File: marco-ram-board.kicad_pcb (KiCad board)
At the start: 4 copper layers, 160 x 100 mm, 185 parts, among them J201 PRG_USB, J202 MCU_RST, J203 MCU_BOOT0, J204 FT_TXD, J205 FT_RXD, J206 CONN_JTAG, J301 CONN_MCU_SERIAL, J302 CONN_EXT, J501 MCU_USB, J502 SD_Card, J503 CONN_DISP, J504 RJ45_Amphenol_RJMG1BD3B8K1ANR, J601 CONN_JACK_12V, J602 CONN_SCREW_12V, Q201 MMBT3906, Q601 DMP3037LSS, SW301 SW_RST, SW302 SW_BOOT0, SW501 BTN0, SW502 BTN1, SW503 BTN2, SW504 BTN3, SW601 PWR_SW, U201 FT2232HL, U301 STM32F765IITx, U401 IS42S86400D, U402 IS42S86400D, U403 IS42S86400D, U404 IS42S86400D, U405 IS42S86400D, U406 IS42S86400D, U407 IS42S86400D, U408 IS42S86400D, U501 KSZ8081RNA, U601 LM2576S-3.3, Y201 12MHz, Y301 25MHz

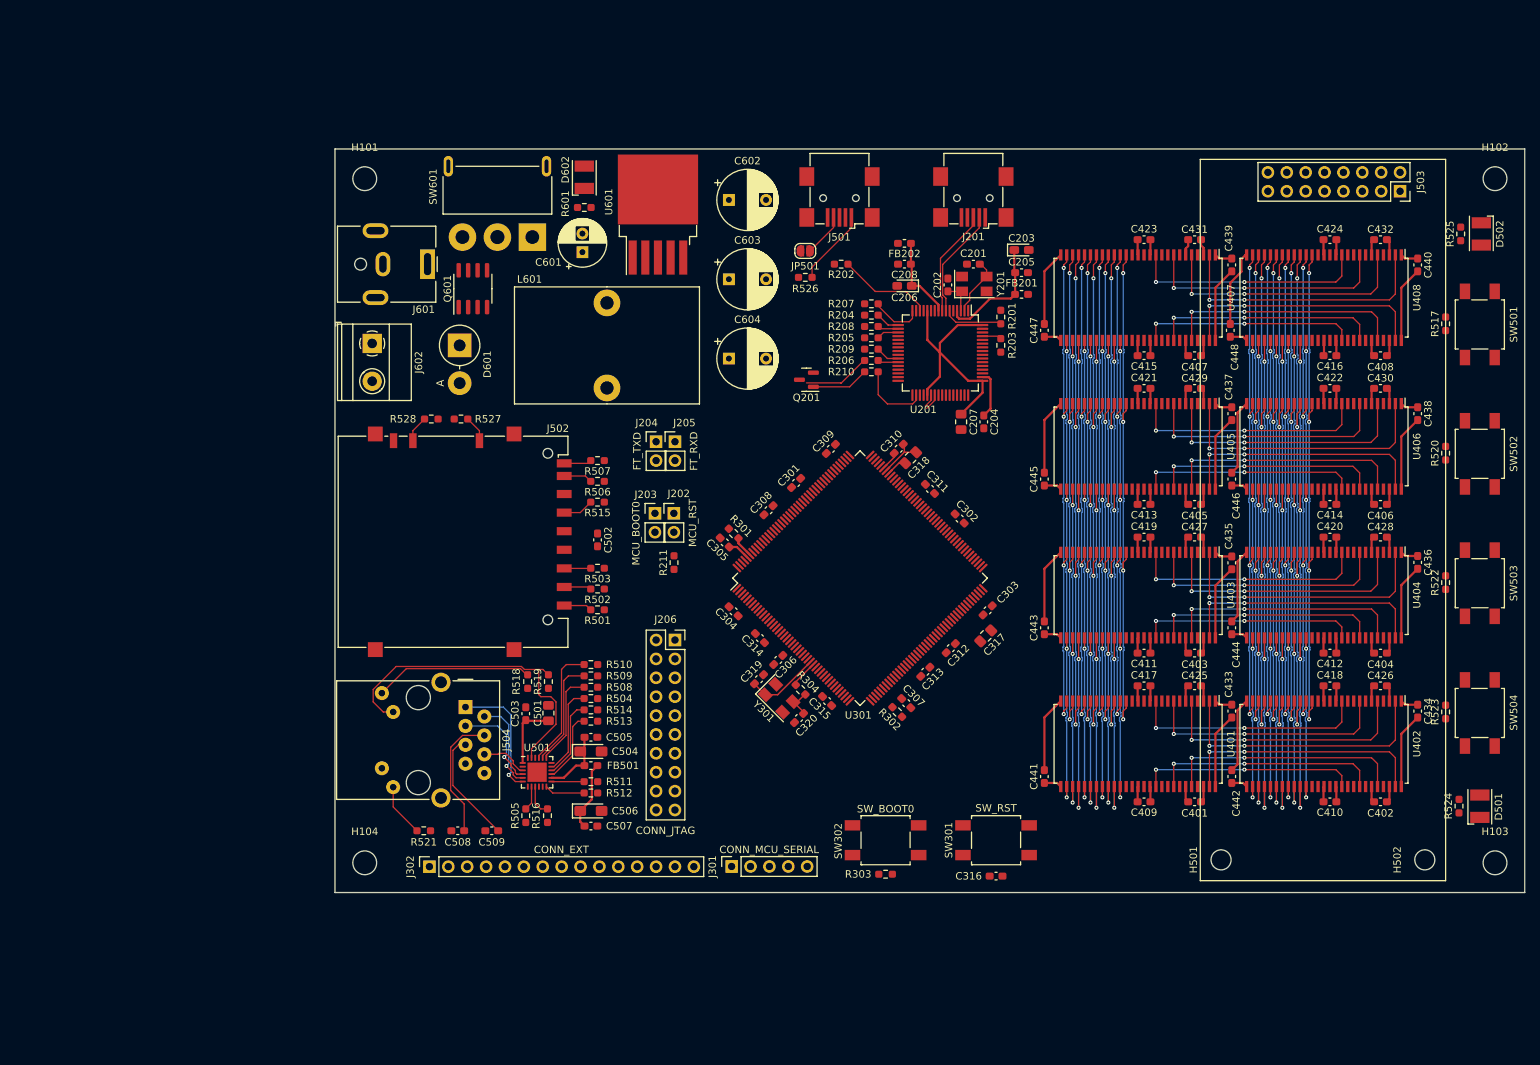
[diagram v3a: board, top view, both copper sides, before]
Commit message: Small placement modifications, change most routing to .2mm, more RAM routing
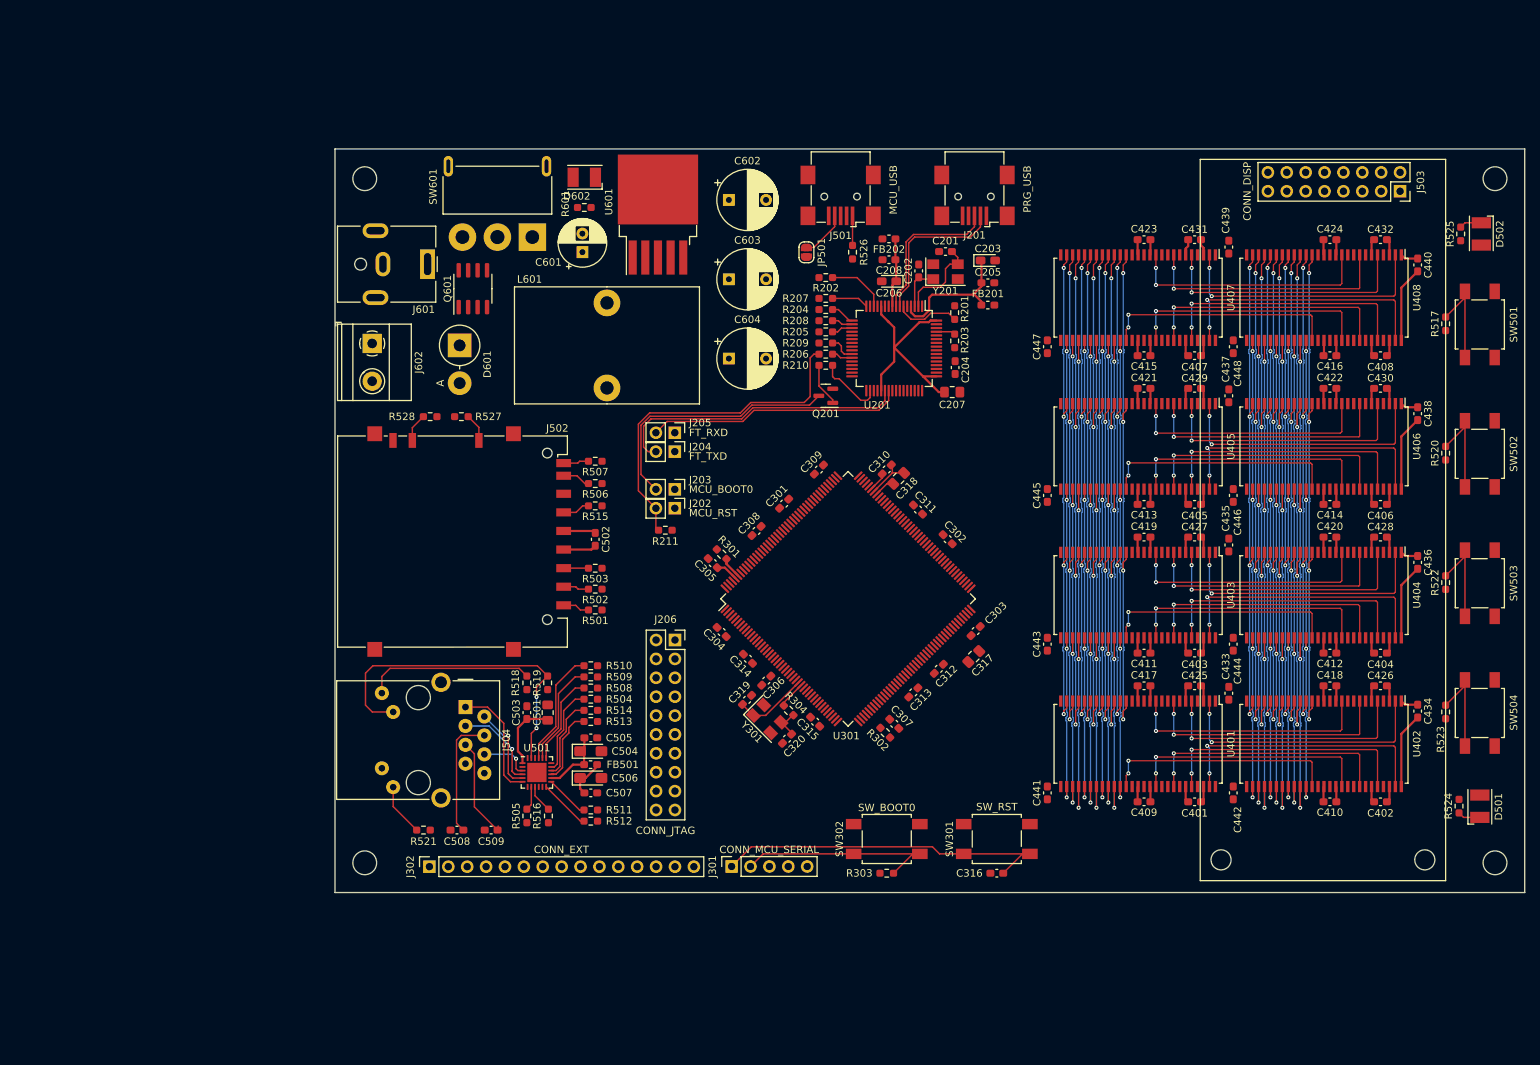
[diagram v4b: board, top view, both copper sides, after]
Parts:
- moved C204 8.26 mm to (153.4, 69.4)
- moved R526 7.20 mm to (139.6, 53.9), turned to 90 degrees
- moved U201 6.23 mm to (145.2, 66.8)
- moved R201 6.23 mm to (153.3, 62.0)
- moved R203 6.23 mm to (153.3, 65.8)
- moved R210 6.20 mm to (136.0, 69.1)
- moved R206 6.19 mm to (136.0, 67.6)
- moved R209 6.19 mm to (136.0, 66.1)
- moved R205 6.19 mm to (136.0, 64.6)
- moved R208 6.18 mm to (136.0, 63.1)
- moved R204 6.18 mm to (136.0, 61.6)
- moved R207 6.18 mm to (136.0, 60.1)
- moved FB201 4.75 mm to (157.8, 61.0)
- moved C203 4.74 mm to (157.8, 55.0)
- moved C205 4.73 mm to (157.8, 58.0)
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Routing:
- net VDD: track 189.9 -> 95.6 mm
- net GND: track 174.2 -> 117.9 mm
- net /mcu/~{RESET}: track 0.00 -> 46.3 mm
- net Net-(J204-Pad2): track 1.11 -> 39.9 mm
- net Net-(J202-Pad2): track 8.99 -> 46.6 mm
- net Net-(J203-Pad2): track 0.00 -> 35.0 mm
- net Net-(J205-Pad2): track 1.53 -> 34.4 mm
- net /mcu/SDRAM.~{BL1}: track 0.00 -> 31.6 mm, vias 0 -> 2
- net /mcu/SDRAM.~{BL0}: track 0.00 -> 31.6 mm, vias 0 -> 2
- net /mcu/SDRAM.~{BL3}: track 0.00 -> 31.6 mm, vias 0 -> 2
- net /mcu/SDRAM.~{BL2}: track 0.00 -> 31.6 mm, vias 0 -> 2
- net /mcu/BOOT0: track 0.00 -> 28.1 mm
- net /mcu-if/BTN2: track 0.00 -> 13.4 mm
- net /mcu-if/BTN0: track 0.00 -> 13.4 mm
- net /mcu-if/BTN1: track 0.00 -> 13.4 mm
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
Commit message: Finish RAM routing (except connections to MCU).
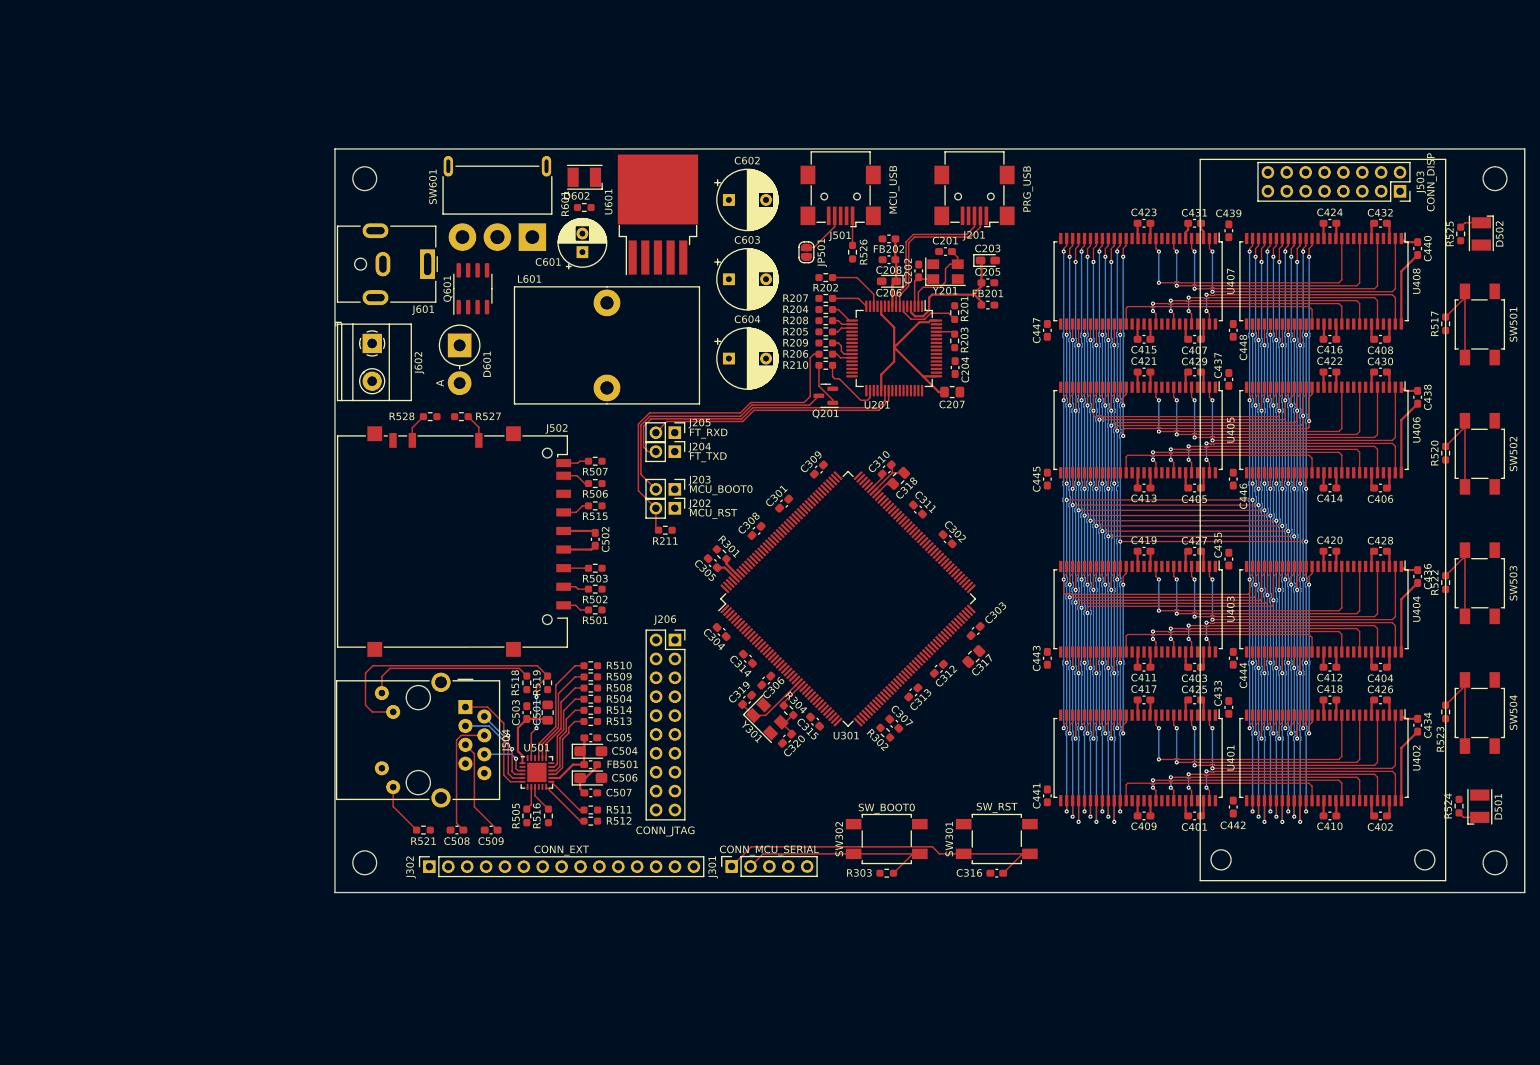
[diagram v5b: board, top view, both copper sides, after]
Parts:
- moved C405 2.20 mm to (185.6, 85.6)
- moved C406 2.20 mm to (210.6, 85.6)
- moved C407 2.20 mm to (185.6, 65.6)
- moved C408 2.20 mm to (210.6, 65.6)
- moved C413 2.20 mm to (178.8, 85.6)
- moved C414 2.20 mm to (203.8, 85.6)
- moved C415 2.20 mm to (178.8, 65.6)
- moved C416 2.20 mm to (203.8, 65.6)
- moved C421 2.20 mm to (178.8, 70.0)
- moved C422 2.20 mm to (203.8, 70.0)
- moved C423 2.20 mm to (178.8, 50.0)
- moved C424 2.20 mm to (203.8, 50.0)
- moved C429 2.20 mm to (185.6, 70.0)
- moved C430 2.20 mm to (210.6, 70.0)
- moved C431 2.20 mm to (185.6, 50.0)
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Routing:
- net /mcu/SDRAM.A3: track 135.8 -> 173.1 mm
- net /mcu/SDRAM.~{CAS}: track 136.3 -> 173.5 mm, vias 8 -> 9
- net /mcu/SDRAM.A0: track 136.3 -> 173.4 mm, vias 8 -> 9
- net /mcu/SDRAM.A10: track 141.9 -> 178.9 mm, vias 8 -> 9
- net /mcu/SDRAM.BA0: track 136.3 -> 172.3 mm, vias 8 -> 9
- net /mcu/SDRAM.A2: track 141.9 -> 177.1 mm, vias 8 -> 9
- net /mcu/SDRAM.BA1: track 147.5 -> 182.5 mm
- net /mcu/SDRAM.~{RAS}: track 147.5 -> 182.5 mm, vias 8 -> 9
- net /mcu/SDRAM.A7: track 132.6 -> 167.5 mm, vias 8 -> 10
- net /mcu/SDRAM.A1: track 147.5 -> 182.4 mm, vias 8 -> 9
- net /mcu/SDRAM.A5: track 138.2 -> 171.6 mm, vias 8 -> 10
- net /mcu/SDRAM.A4: track 132.6 -> 165.9 mm, vias 8 -> 10
- net /mcu/SDRAM.A12: track 138.2 -> 171.5 mm, vias 8 -> 10
- net /mcu/SDRAM.A11: track 132.6 -> 165.9 mm, vias 8 -> 10
- net /mcu/SDRAM.CLK: track 132.6 -> 165.2 mm, vias 8 -> 9
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
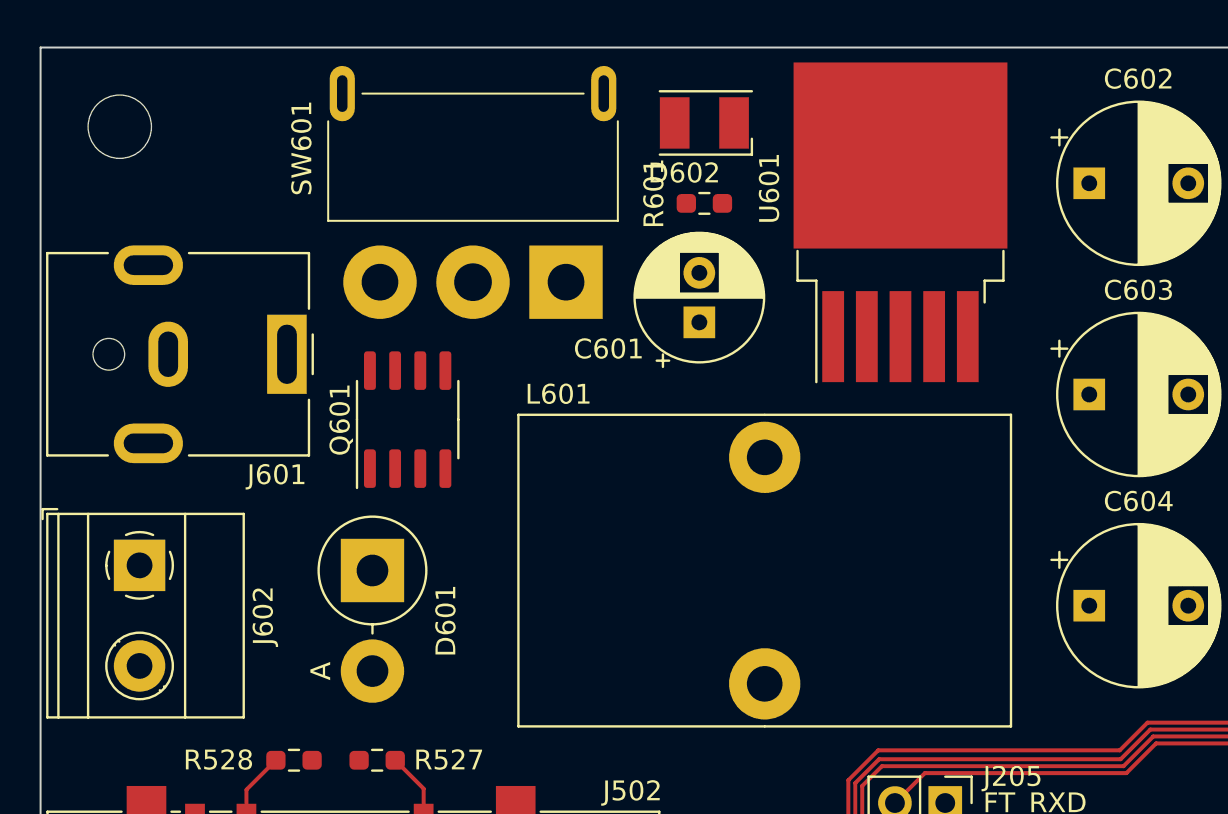
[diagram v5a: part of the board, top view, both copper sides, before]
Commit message: Route power supply
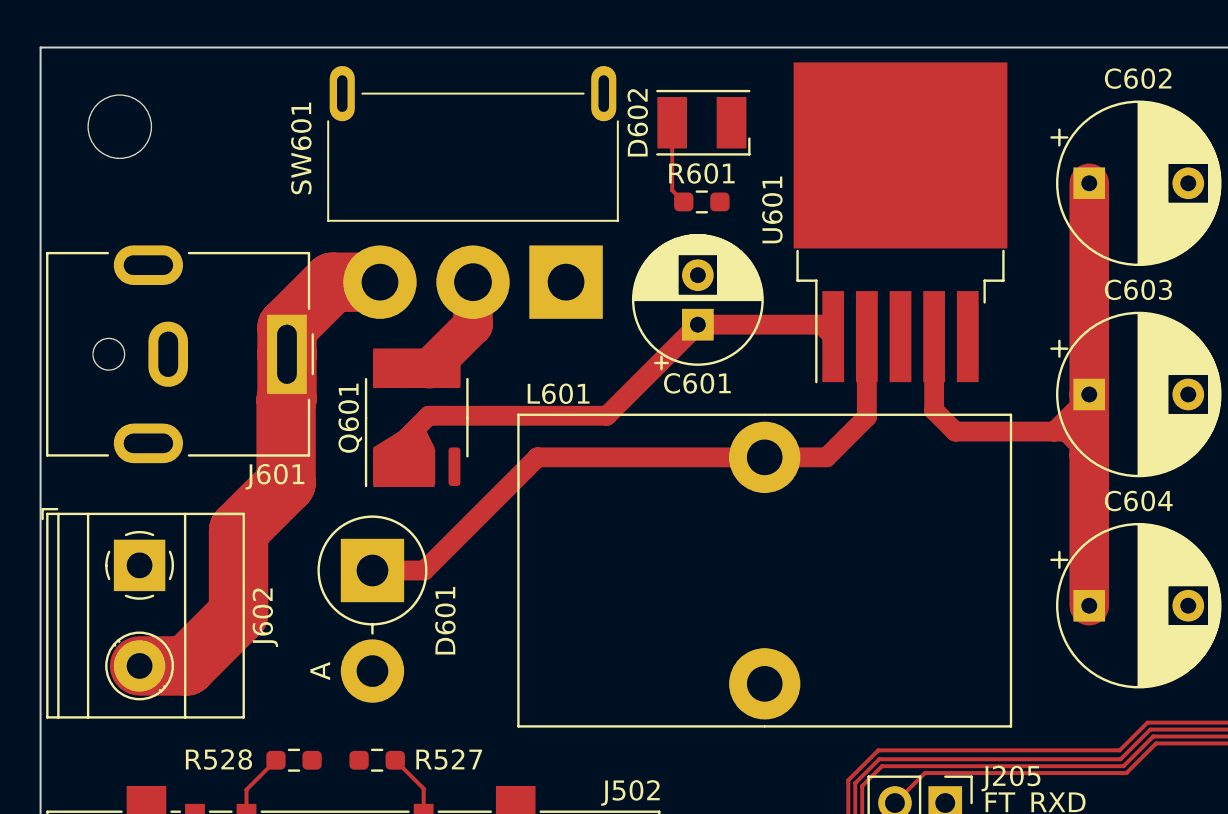
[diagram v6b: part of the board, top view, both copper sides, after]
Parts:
- moved Q601 0.47 mm to (89.0, 58.7)
- moved R601 0.15 mm to (103.4, 47.8), turned to 180 degrees
- moved C601 0.14 mm to (103.2, 54.0)
- moved D602 0.13 mm to (103.4, 43.8)
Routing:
- net VDD: track 95.3 -> 131.7 mm
- net Net-(D601-Pad1): track 0.00 -> 32.2 mm
- net Net-(C601-Pad1): track 0.00 -> 28.2 mm
- net Net-(J601-Pad1): track 0.00 -> 27.2 mm
- net Net-(Q601-Pad5): track 0.00 -> 9.10 mm
- net Net-(D602-Pad2): track 0.00 -> 4.24 mm

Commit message: Update layout from schematic to propagate effects of commit b3d85d6.
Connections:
- U301 pad 32: /mcu/SDRAM.~{WE} -> unconnected-(U301-Pad32)
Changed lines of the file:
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@@
   (net 242 "/mcu/SDRAM.D16")
   (net 243 "/mcu/SDRAM.D18")
+  (net 244 "unconnected-(U301-Pad32)")
   (footprint "Capacitor_THT:CP_Radial_D8.0mm_P5.00mm" (layer "F.Cu")
     (at 122.969349 68.194)
@@
       (net 8 "/mcu/~{RESET}") (pinfunction "NRST") (pintype "input"))
     (pad "32" smd roundrect (at -12.675 4.75 45) (size 1.5 0.3) (layers "F.Cu" "F.Paste" "F.Mask") (roundrect_rratio 0.25)
-      (net 167 "/mcu/SDRAM.~{WE}") (pinfunction "PC0") (pintype "bidirectional"))
+      (net 244 "unconnected-(U301-Pad32)") (pinfunction "PC0") (pintype "bidirectional"))
     (pad "33" smd roundrect (at -12.675 5.25 45) (size 1.5 0.3) (layers "F.Cu" "F.Paste" "F.Mask") (roundrect_rratio 0.25)
       (net 168 "/mcu-if/RMII.MDC") (pinfunction "PC1") (pintype "bidirectional"))
